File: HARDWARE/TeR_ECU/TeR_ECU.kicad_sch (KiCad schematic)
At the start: 3 parts, among them U7 HDSP-A153

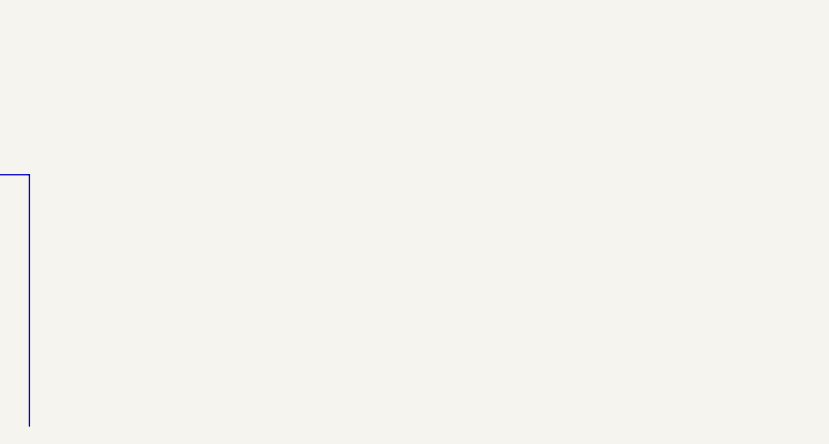
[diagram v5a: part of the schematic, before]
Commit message: Finished re layout and adaption between the two versions
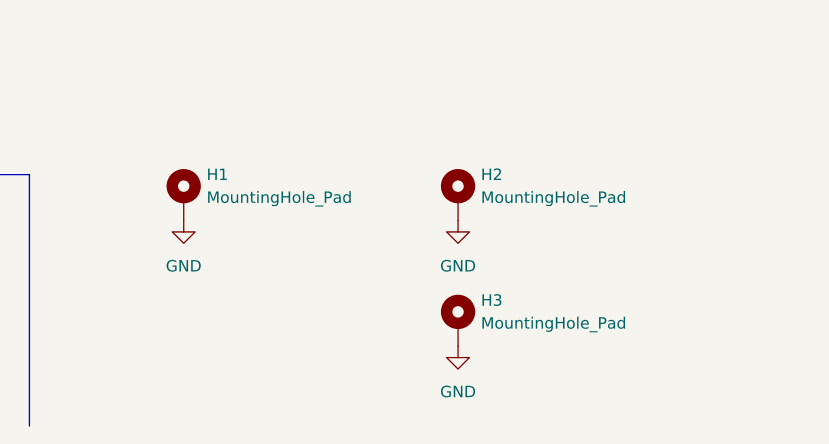
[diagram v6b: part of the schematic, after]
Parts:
- added H1, H2, H3: MountingHole_Pad, MountingHole:MountingHole_3.2mm_M3_ISO7380_Pad_TopBottom, symbol Mechanical:MountingHole_Pad
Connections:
- net GND: now also H1.1, H2.1, H3.1
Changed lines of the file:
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@@
+    )
+  )
+  (symbol (lib_id "power:GND") (at 81.28 173.99 0) (unit 1)
+    (in_bom yes) (on_board yes) (dnp no) (fields_autoplaced)
+    (property "Reference" "#PWR011" (at 81.28 180.34 0)
+      (effects (font (size 1.27 1.27)) hide)
+    )
+    (property "Value" "GND" (at 81.28 179.07 0)
+      (effects (font (size 1.27 1.27)))
+    )
+    (property "Footprint" "" (at 81.28 173.99 0)
+      (effects (font (size 1.27 1.27)) hide)
+    )
+    (property "Datasheet" "" (at 81.28 173.99 0)
+      (effects (font (size 1.27 1.27)) hide)
+    )
+    (pin "1")
+    (instances
+      (project "TeR_ECU"
+        (path "/84413845-c4f3-4743-bcd2-a67649c90902"
+          (reference "#PWR011") (unit 1)
+        )
+      )
     )
   )
@@
         (path "/84413845-c4f3-4743-bcd2-a67649c90902"
           (reference "#PWR03") (unit 1)
+        )
+      )
+    )
+  )
+  (symbol (lib_id "Mechanical:MountingHole_Pad") (at 81.28 171.45 0) (unit 1)
+    (in_bom yes) (on_board yes) (dnp no) (fields_autoplaced)
+    (property "Reference" "H1" (at 83.82 168.91 0)
+      (effects (font (size 1.27 1.27)) (justify left))
+    )
+    (property "Value" "MountingHole_Pad" (at 83.82 171.45 0)
+      (effects (font (size 1.27 1.27)) (justify left))
+    )
+    (property "Footprint" "MountingHole:MountingHole_3.2mm_M3_ISO7380_Pad_TopBottom" (at 81.28 171.45 0)
+      (effects (font (size 1.27 1.27)) hide)
+    )
+    (property "Datasheet" "~" (at 81.28 171.45 0)
+      (effects (font (size 1.27 1.27)) hide)
+    )
+    (pin "1")
+    (instances
+      (project "TeR_ECU"
+        (path "/84413845-c4f3-4743-bcd2-a67649c90902"
+          (reference "H1") (unit 1)
         )
       )
@@
         (path "/84413845-c4f3-4743-bcd2-a67649c90902"
           (reference "R3") (unit 1)
+        )
+      )
+    )
+  )
+  (symbol (lib_id "power:GND") (at 111.76 173.99 0) (unit 1)
+    (in_bom yes) (on_board yes) (dnp no) (fields_autoplaced)
+    (property "Reference" "#PWR012" (at 111.76 180.34 0)
+      (effects (font (size 1.27 1.27)) hide)
+    )
+    (property "Value" "GND" (at 111.76 179.07 0)
+      (effects (font (size 1.27 1.27)))
+    )
+    (property "Footprint" "" (at 111.76 173.99 0)
+      (effects (font (size 1.27 1.27)) hide)
+    )
+    (property "Datasheet" "" (at 111.76 173.99 0)
+      (effects (font (size 1.27 1.27)) hide)
+    )
+    (pin "1")
+    (instances
+      (project "TeR_ECU"
+        (path "/84413845-c4f3-4743-bcd2-a67649c90902"
+          (reference "#PWR012") (unit 1)
         )
       )
@@
     )
   )
+  (symbol (lib_id "Mechanical:MountingHole_Pad") (at 111.76 171.45 0) (unit 1)
+    (in_bom yes) (on_board yes) (dnp no) (fields_autoplaced)
+    (property "Reference" "H2" (at 114.3 168.91 0)
+      (effects (font (size 1.27 1.27)) (justify left))
+    )
+    (property "Value" "MountingHole_Pad" (at 114.3 171.45 0)
+      (effects (font (size 1.27 1.27)) (justify left))
+    )
+    (property "Footprint" "MountingHole:MountingHole_3.2mm_M3_ISO7380_Pad_TopBottom" (at 111.76 171.45 0)
+      (effects (font (size 1.27 1.27)) hide)
+    )
+    (property "Datasheet" "~" (at 111.76 171.45 0)
+      (effects (font (size 1.27 1.27)) hide)
+    )
+    (pin "1")
+    (instances
+      (project "TeR_ECU"
+        (path "/84413845-c4f3-4743-bcd2-a67649c90902"
+          (reference "H2") (unit 1)
+        )
+      )
+    )
+  )
   (symbol (lib_id "power:GND") (at 202.565 77.47 90) (unit 1)
     (in_bom yes) (on_board yes) (dnp no) (fields_autoplaced)
@@
     )
   )
+  (symbol (lib_id "Mechanical:MountingHole_Pad") (at 111.76 185.42 0) (unit 1)
+    (in_bom yes) (on_board yes) (dnp no) (fields_autoplaced)
+    (property "Reference" "H3" (at 114.3 182.88 0)
+      (effects (font (size 1.27 1.27)) (justify left))
+    )
+    (property "Value" "MountingHole_Pad" (at 114.3 185.42 0)
+      (effects (font (size 1.27 1.27)) (justify left))
+    )
+    (property "Footprint" "MountingHole:MountingHole_3.2mm_M3_ISO7380_Pad_TopBottom" (at 111.76 185.42 0)
+      (effects (font (size 1.27 1.27)) hide)
+    )
+    (property "Datasheet" "~" (at 111.76 185.42 0)
+      (effects (font (size 1.27 1.27)) hide)
+    )
+    (pin "1")
+    (instances
+      (project "TeR_ECU"
+        (path "/84413845-c4f3-4743-bcd2-a67649c90902"
+          (reference "H3") (unit 1)
+        )
+      )
+    )
+  )
   (symbol (lib_id "power:GND") (at 48.26 186.69 90) (unit 1)
     (in_bom yes) (on_board yes) (dnp no) (fields_autoplaced)
@@
         )
       )
+    )
+  )
+  (symbol (lib_id "power:GND") (at 111.76 187.96 0) (unit 1)
+    (in_bom yes) (on_board yes) (dnp no) (fields_autoplaced)
+    (property "Reference" "#PWR014" (at 111.76 194.31 0)
+      (effects (font (size 1.27 1.27)) hide)
+    )
+    (property "Value" "GND" (at 111.76 193.04 0)
+      (effects (font (size 1.27 1.27)))
+    )
+    (property "Footprint" "" (at 111.76 187.96 0)
+      (effects (font (size 1.27 1.27)) hide)
+    )
+    (property "Datasheet" "" (at 111.76 187.96 0)
+      (effects (font (size 1.27 1.27)) hide)
+    )
+    (pin "1")
+    (instances
+      (project "TeR_ECU"
+        (path "/84413845-c4f3-4743-bcd2-a67649c90902"
+          (reference "#PWR014") (unit 1)
+        )
+      )

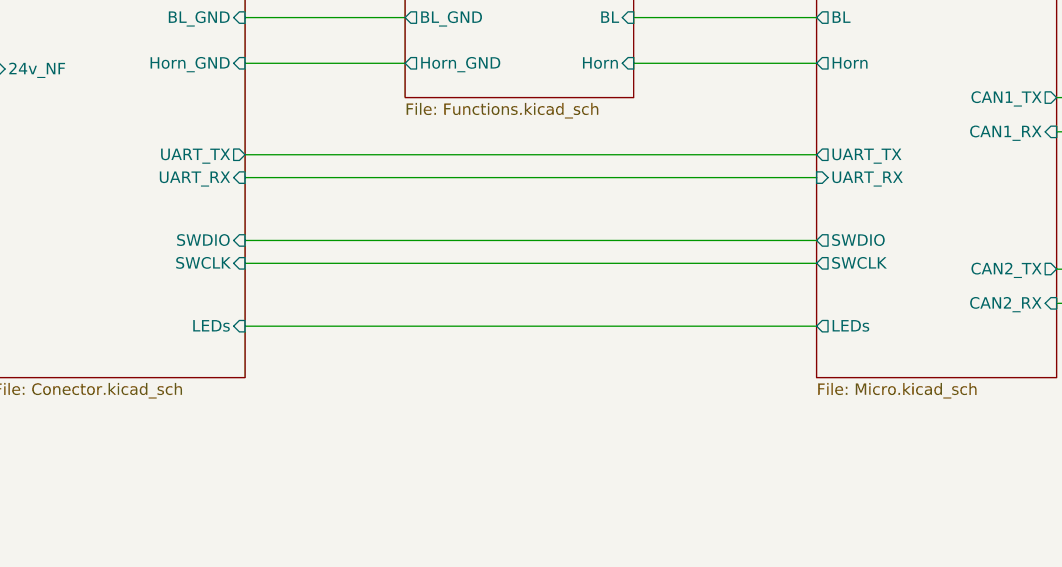
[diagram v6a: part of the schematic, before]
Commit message: Removed unnecesary via, DRC:Passes
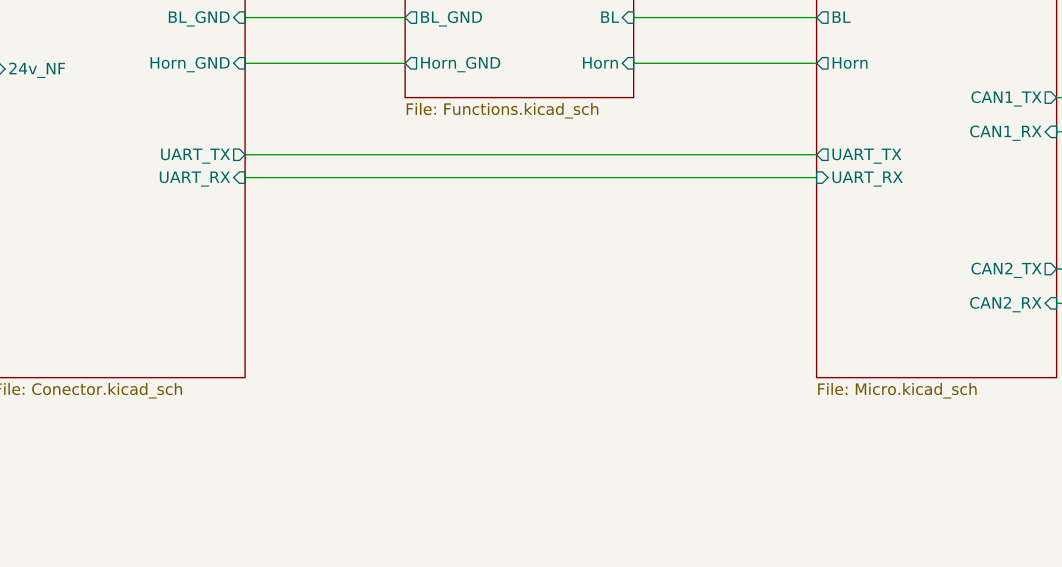
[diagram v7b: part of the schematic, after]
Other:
- sheet Conector ports: added none; removed LEDs, SWCLK, SWDIO
- sheet Micro ports: added none; removed LEDs, SWCLK, SWDIO
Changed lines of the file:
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@@
-    (stroke (width 0) (type default))
-  )
-  (wire (pts (xy 66.04 134.62) (xy 129.54 134.62))
     (stroke (width 0) (type default))
   )
@@
     (stroke (width 0) (type default))
   )
-  (wire (pts (xy 66.04 127.635) (xy 129.54 127.635))
-    (stroke (width 0) (type default))
-  )
   (wire (pts (xy 179.705 60.96) (xy 186.69 60.96))
-    (stroke (width 0) (type default))
-  )
-  (wire (pts (xy 66.04 125.095) (xy 129.54 125.095))
     (stroke (width 0) (type default))
   )
@@
       (effects (font (size 1.27 1.27)) (justify left))
     )
-    (pin "LEDs" output (at 129.54 134.62 180)
-      (effects (font (size 1.27 1.27)) (justify left))
-    )
-    (pin "SWCLK" output (at 129.54 127.635 180)
-      (effects (font (size 1.27 1.27)) (justify left))
-    )
-    (pin "SWDIO" output (at 129.54 125.095 180)
-      (effects (font (size 1.27 1.27)) (justify left))
-    )
     (pin "UART_RX" input (at 129.54 118.11 180)
       (effects (font (size 1.27 1.27)) (justify left))
@@
       (effects (font (size 1.27 1.27)) (justify right))
     )
-    (pin "LEDs" input (at 66.04 134.62 0)
-      (effects (font (size 1.27 1.27)) (justify right))
-    )
-    (pin "SWCLK" input (at 66.04 127.635 0)
-      (effects (font (size 1.27 1.27)) (justify right))
-    )
-    (pin "SWDIO" input (at 66.04 125.095 0)
-      (effects (font (size 1.27 1.27)) (justify right))
-    )

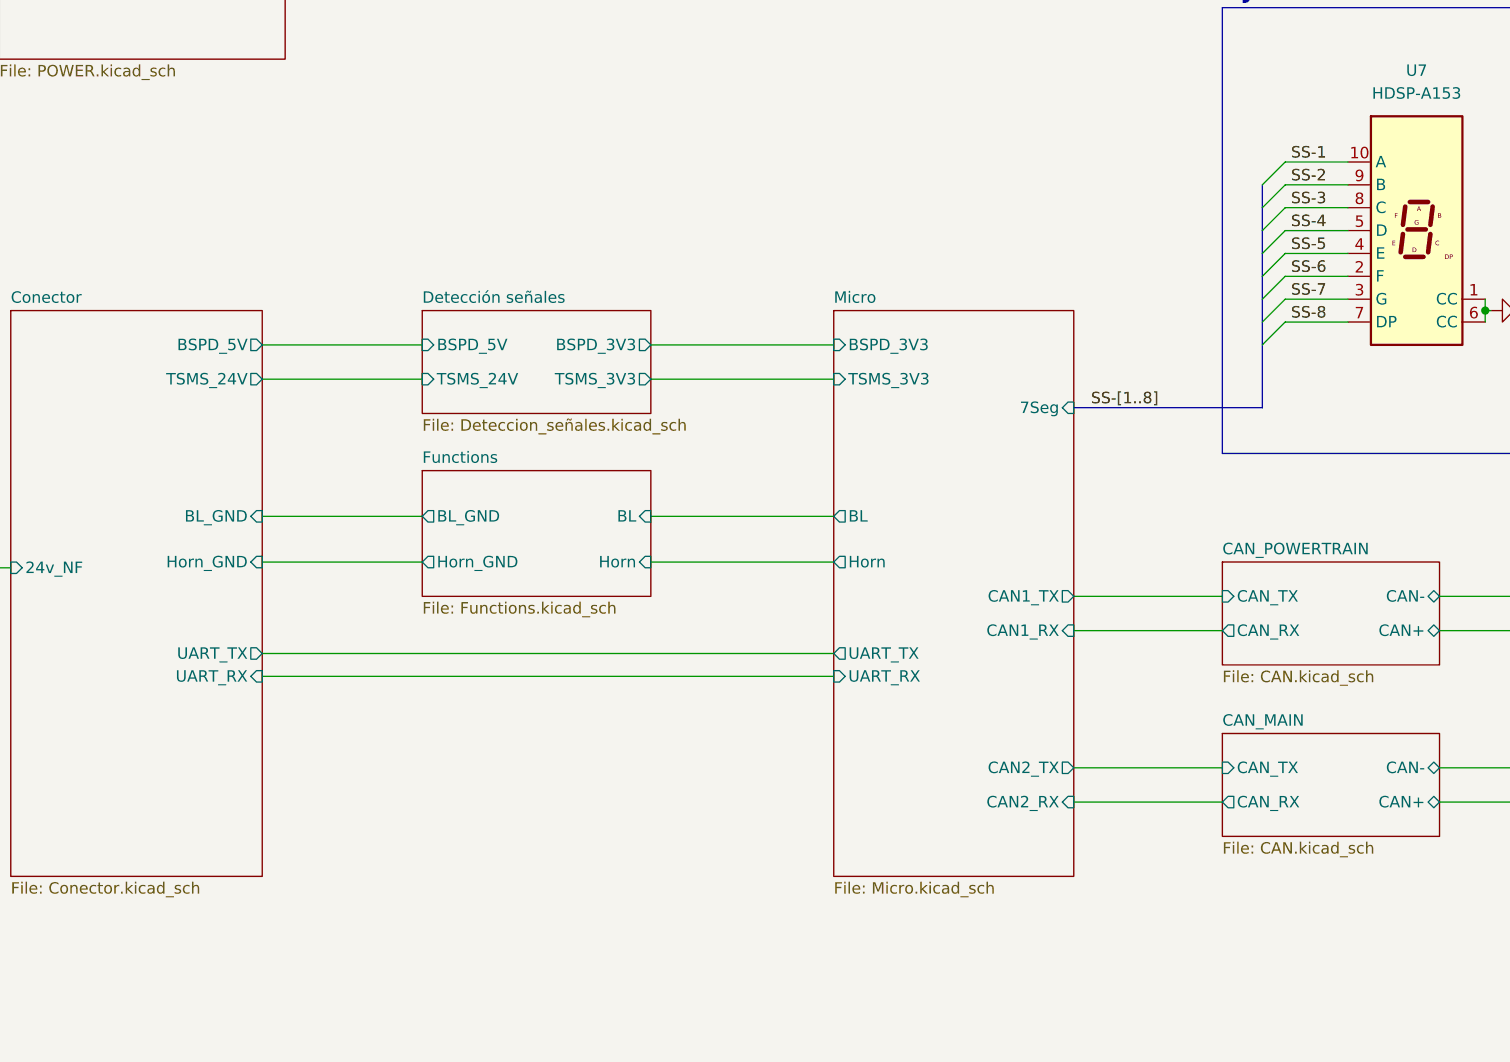
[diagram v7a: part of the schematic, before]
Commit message: Microcontroller f405 sketch started
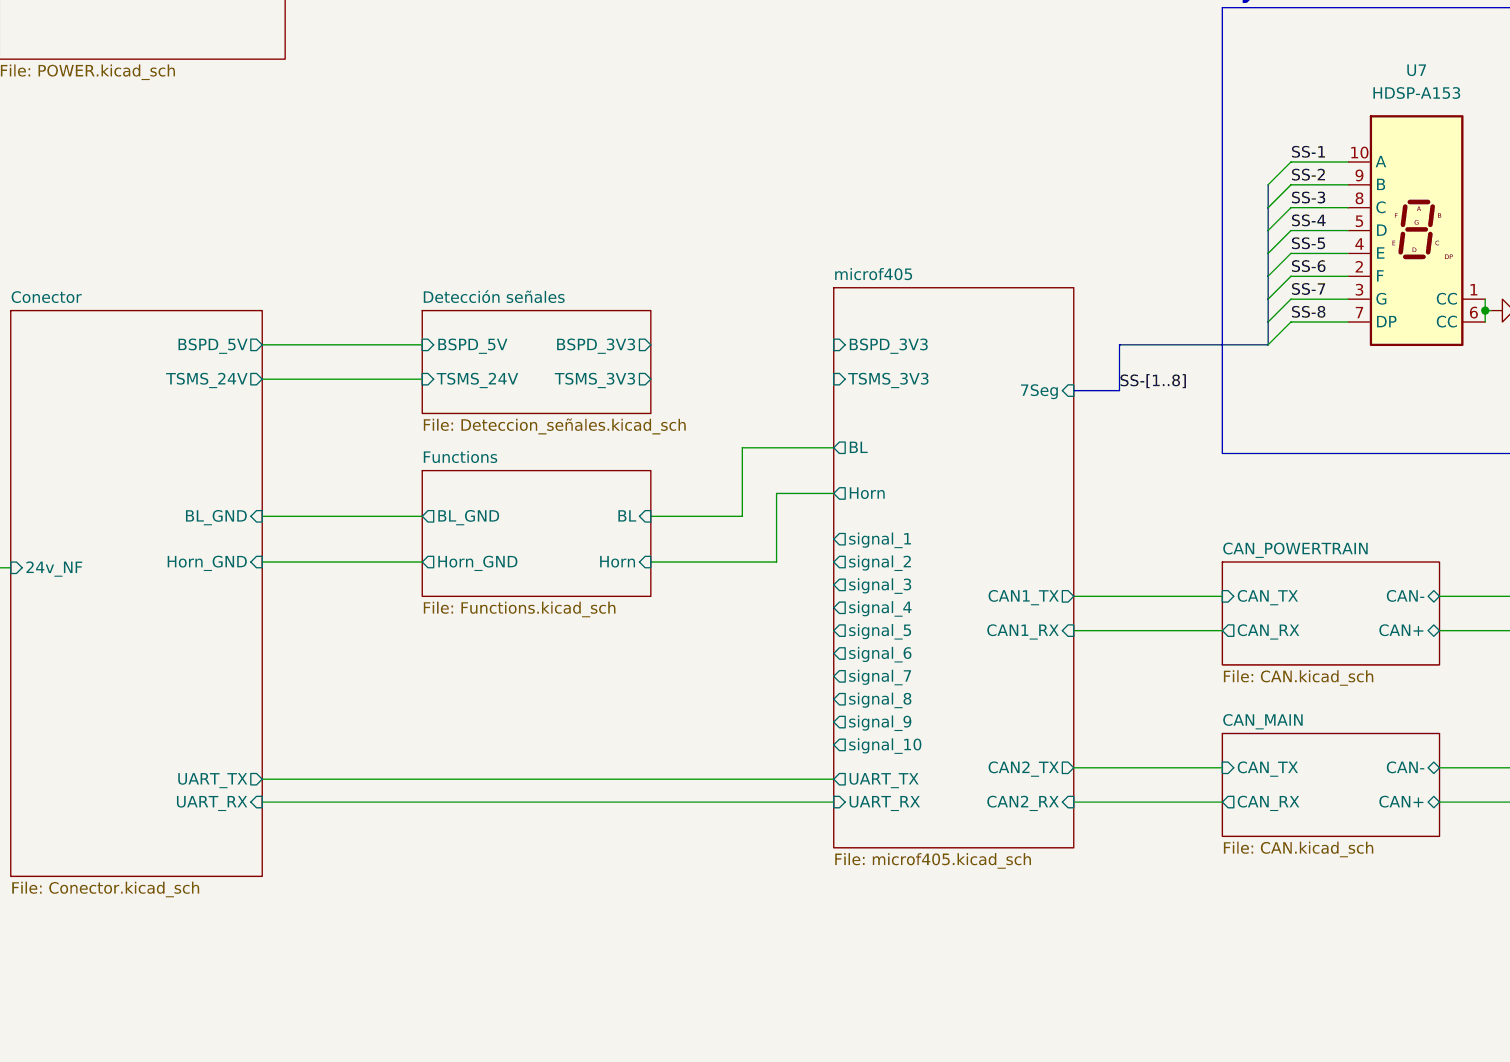
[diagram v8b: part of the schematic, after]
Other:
- removed sheet Micro
- added sheet microf405 (microf405.kicad_sch)
